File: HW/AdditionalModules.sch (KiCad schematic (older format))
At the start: 25 parts, among them J40 ph_1x2, Q40 BC817, Q41 BC817, U10 PCA9633DP1, U40 AT_CryptoAuth, U41 HIH8000_I2C

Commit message: Updates components to add manufacturer, part number, ... fields. Also checked some values.
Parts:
- C10: symbol Device:C -> calin:C; characteristics (none) -> 100 nF / 50V / X7R; manufacturer (none) -> Samsung; package (none) -> 0805; part-number (none) -> CL21B104KBCNNNC
- C11: value 1uF -> 4,7uF; symbol Device:C -> calin:C; characteristics (none) -> 4.7 µF / 16 V / X7R; manufacturer (none) -> AVX; package (none) -> 0805; part-number (none) -> 0805YC475KAT2A
- C40: symbol Device:C -> calin:C; Variant (none) -> ATCrypto; characteristics (none) -> 100 nF / 50V / X7R; manufacturer (none) -> Samsung; package (none) -> 0805; part-number (none) -> CL21B104KBCNNNC
- C41, C42: symbol Device:C -> calin:C; Variant (none) -> HIH; characteristics (none) -> 100 nF / 50V / X7R; manufacturer (none) -> Samsung; package (none) -> 0805; part-number (none) -> CL21B104KBCNNNC
- Q40, Q41: characteristics (none) -> BC817-40; manufacturer (none) -> Diodes; package (none) -> SOT-23; part-number (none) -> BC817-40Q
- R10, R11, R12, R13: characteristics (none) -> 100 1%; manufacturer (none) -> Panasonic; package (none) -> 0805; part-number (none) -> ERJ-6ENF1000V
- R40, R41: value 10K -> 10k; characteristics (none) -> 10k; manufacturer (none) -> Vishay; package (none) -> 0805; part-number (none) -> CRCW080510K0FKEA
- SYM10, SYM11, SYM12, SYM13: characteristics (none) -> LightPipe; manufacturer (none) -> BIVAR; package (none) -> SLP3-XXX-XXX-X; part-number (none) -> SLP3-150-xxx-F
- U10: characteristics (none) -> 4-bit Fm+ I2C-bus LED driver; manufacturer (none) -> NXP Semiconductors; package (none) -> TSSOP8 (SOT505-1); part-number (none) -> PCA9633DP1
- U40: Variant (none) -> ATCrypto; characteristics (none) -> *; manufacturer (none) -> Microchip; package (none) -> SOIC-8 3.90mm; part-number (none) -> ATSHA204A/ATECC508A/ATECC608A-SSHDA
- U41: Variant (none) -> HIH; characteristics (none) -> +/- 2.0 RH Accuracy; manufacturer (none) -> Honeywell; package (none) -> SOIC-8 3.90mm; part-number (none) -> HIH8130-021-001 / HIH8131-021-001
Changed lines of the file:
@@
 Sheet 3 3
 Title "ESP32 RFM69/RFM9x Gateway"
-Date "2019-04-25"
-Rev "32"
+Date "2019-05-02"
+Rev "33"
 Comp "Calin Radoni"
 Comment1 ""
@@
 F 2 "CalinGeneric:SOIC-8-HS" H 2200 4450 50  0001 C CNN
 F 3 "" H 2200 4450 50  0001 C CNN
+F 4 "ATCrypto" H 0   0   50  0001 C CNN "Variant"
+F 5 "ATSHA204A/ATECC508A/ATECC608A-SSHDA" H 0   0   50  0001 C CNN "part-number"
+F 6 "*" H 0   0   50  0001 C CNN "characteristics"
+F 7 "Microchip" H 0   0   50  0001 C CNN "manufacturer"
+F 8 "SOIC-8 3.90mm" H 0   0   50  0001 C CNN "package"
 	1    2200 4450
 	1    0    0    -1
 $EndComp
 $Comp
-L Device:C C?
+L calin:C C?
 U 1 1 5CCB0E9E
 P 1350 4450
@@
 F 2 "CalinGeneric:C0805HS" H 1388 4300 50  0001 C CNN
 F 3 "" H 1350 4450 50  0000 C CNN
+F 4 "ATCrypto" H 0   0   50  0001 C CNN "Variant"
+F 5 "100 nF / 50V / X7R" H 0   0   50  0001 C CNN "characteristics"
+F 6 "Samsung" H 0   0   50  0001 C CNN "manufacturer"
+F 7 "0805" H 0   0   50  0001 C CNN "package"
+F 8 "CL21B104KBCNNNC" H 0   0   50  0001 C CNN "part-number"
 	1    1350 4450
 	1    0    0    -1
@@
 F 2 "CalinGeneric:R0805HS" V 8430 1200 30  0001 C CNN
 F 3 "" H 8500 1200 30  0000 C CNN
+F 4 "100 1%" H 0   0   50  0001 C CNN "characteristics"
+F 5 "Panasonic" H 0   0   50  0001 C CNN "manufacturer"
+F 6 "0805" H 0   0   50  0001 C CNN "package"
+F 7 "ERJ-6ENF1000V" H 0   0   50  0001 C CNN "part-number"
 	1    8500 1200
 	0    1    1    0
@@
 F 2 "CalinGeneric:R0805HS" V 8430 1500 30  0001 C CNN
 F 3 "" H 8500 1500 30  0000 C CNN
+F 4 "100 1%" H 0   0   50  0001 C CNN "characteristics"
+F 5 "Panasonic" H 0   0   50  0001 C CNN "manufacturer"
+F 6 "0805" H 0   0   50  0001 C CNN "package"
+F 7 "ERJ-6ENF1000V" H 0   0   50  0001 C CNN "part-number"
 	1    8500 1500
 	0    1    1    0
@@
 F 2 "CalinGeneric:R0805HS" V 8430 1800 30  0001 C CNN
 F 3 "" H 8500 1800 30  0000 C CNN
+F 4 "100 1%" H 0   0   50  0001 C CNN "characteristics"
+F 5 "Panasonic" H 0   0   50  0001 C CNN "manufacturer"
+F 6 "0805" H 0   0   50  0001 C CNN "package"
+F 7 "ERJ-6ENF1000V" H 0   0   50  0001 C CNN "part-number"
 	1    8500 1800
 	0    1    1    0
@@
 F 2 "CalinGeneric:R0805HS" V 8430 2100 30  0001 C CNN
 F 3 "" H 8500 2100 30  0000 C CNN
+F 4 "100 1%" H 0   0   50  0001 C CNN "characteristics"
+F 5 "Panasonic" H 0   0   50  0001 C CNN "manufacturer"
+F 6 "0805" H 0   0   50  0001 C CNN "package"
+F 7 "ERJ-6ENF1000V" H 0   0   50  0001 C CNN "part-number"
 	1    8500 2100
 	0    1    1    0
@@
 F 2 "CalinGeneric:SLP3-xxx-150-x" H 9800 1200 50  0001 C CNN
 F 3 "" V 9800 1200 50  0001 C CNN
+F 4 "LightPipe" H 0   0   50  0001 C CNN "characteristics"
+F 5 "BIVAR" H 0   0   50  0001 C CNN "manufacturer"
+F 6 "SLP3-XXX-XXX-X" H 0   0   50  0001 C CNN "package"
+F 7 "SLP3-150-xxx-F" H 0   0   50  0001 C CNN "part-number"
 	1    9800 1200
 	1    0    0    -1
@@
 F 2 "CalinGeneric:SLP3-xxx-150-x" H 9800 1500 50  0001 C CNN
 F 3 "" V 9800 1500 50  0001 C CNN
+F 4 "LightPipe" H 0   0   50  0001 C CNN "characteristics"
+F 5 "BIVAR" H 0   0   50  0001 C CNN "manufacturer"
+F 6 "SLP3-XXX-XXX-X" H 0   0   50  0001 C CNN "package"
+F 7 "SLP3-150-xxx-F" H 0   0   50  0001 C CNN "part-number"
 	1    9800 1500
 	1    0    0    -1
@@
 F 2 "CalinGeneric:SLP3-xxx-150-x" H 9800 1800 50  0001 C CNN
 F 3 "" V 9800 1800 50  0001 C CNN
+F 4 "LightPipe" H 0   0   50  0001 C CNN "characteristics"
+F 5 "BIVAR" H 0   0   50  0001 C CNN "manufacturer"
+F 6 "SLP3-XXX-XXX-X" H 0   0   50  0001 C CNN "package"
+F 7 "SLP3-150-xxx-F" H 0   0   50  0001 C CNN "part-number"
 	1    9800 1800
 	1    0    0    -1
@@
 F 2 "CalinGeneric:SLP3-xxx-150-x" H 9800 2100 50  0001 C CNN
 F 3 "" V 9800 2100 50  0001 C CNN
+F 4 "LightPipe" H 0   0   50  0001 C CNN "characteristics"
+F 5 "BIVAR" H 0   0   50  0001 C CNN "manufacturer"
+F 6 "SLP3-XXX-XXX-X" H 0   0   50  0001 C CNN "package"
+F 7 "SLP3-150-xxx-F" H 0   0   50  0001 C CNN "part-number"
 	1    9800 2100
 	1    0    0    -1
@@
 AR Path="/5CCB086C/5CC095F4" Ref="R40"  Part="1"
 F 0 "R40" V 2280 6250 40  0000 C CNN
-F 1 "10K" V 2200 6250 40  0000 C CNN
+F 1 "10k" V 2200 6250 40  0000 C CNN
 F 2 "CalinGeneric:R0805HS" V 2130 6250 30  0001 C CNN
 F 3 "" H 2200 6250 30  0000 C CNN
+F 4 "10k" H 0   0   50  0001 C CNN "characteristics"
+F 5 "Vishay" H 0   0   50  0001 C CNN "manufacturer"
+F 6 "0805" H 0   0   50  0001 C CNN "package"
+F 7 "CRCW080510K0FKEA" H 0   0   50  0001 C CNN "part-number"
 	1    2200 6250
 	0    1    1    0
@@
 AR Path="/5CCB086C/5CC096FF" Ref="R41"  Part="1"
 F 0 "R41" V 2280 6850 40  0000 C CNN
-F 1 "10K" V 2200 6850 40  0000 C CNN
+F 1 "10k" V 2200 6850 40  0000 C CNN
 F 2 "CalinGeneric:R0805HS" V 2130 6850 30  0001 C CNN
 F 3 "" H 2200 6850 30  0000 C CNN
+F 4 "10k" H 0   0   50  0001 C CNN "characteristics"
+F 5 "Vishay" H 0   0   50  0001 C CNN "manufacturer"
+F 6 "0805" H 0   0   50  0001 C CNN "package"
+F 7 "CRCW080510K0FKEA" H 0   0   50  0001 C CNN "part-number"
 	1    2200 6850
 	0    1    1    0
@@
 F 1 "BC817" H 2841 6205 50  0000 L CNN
 F 2 "CalinGeneric:SOT-23" H 2850 6175 50  0001 L CIN
-F 3 "http://www.fairchildsemi.com/ds/BC/BC817.pdf" H 2650 6250 50  0001 L CNN
+F 3 "" H 2650 6250 50  0001 L CNN
+F 4 "BC817-40" H 0   0   50  0001 C CNN "characteristics"
+F 5 "Diodes" H 0   0   50  0001 C CNN "manufacturer"
+F 6 "SOT-23" H 0   0   50  0001 C CNN "package"
+F 7 "BC817-40Q" H 0   0   50  0001 C CNN "part-number"
 	1    2650 6250
 	1    0    0    -1
@@
 F 1 "BC817" H 2841 6895 50  0000 L CNN
 F 2 "CalinGeneric:SOT-23" H 2850 6775 50  0001 L CIN
-F 3 "http://www.fairchildsemi.com/ds/BC/BC817.pdf" H 2650 6850 50  0001 L CNN
+F 3 "" H 2650 6850 50  0001 L CNN
+F 4 "BC817-40" H 0   0   50  0001 C CNN "characteristics"
+F 5 "Diodes" H 0   0   50  0001 C CNN "manufacturer"
+F 6 "SOT-23" H 0   0   50  0001 C CNN "package"
+F 7 "BC817-40Q" H 0   0   50  0001 C CNN "part-number"
 	1    2650 6850
 	1    0    0    1
@@
 F 2 "CalinGeneric:TSSOP8-SOT505-1-HS" H 7700 1650 50  0001 C CNN
 F 3 "" H 7700 1650 50  0001 C CNN
+F 4 "4-bit Fm+ I2C-bus LED driver" H 0   0   50  0001 C CNN "characteristics"
+F 5 "NXP Semiconductors" H 0   0   50  0001 C CNN "manufacturer"
+F 6 "TSSOP8 (SOT505-1)" H 0   0   50  0001 C CNN "package"
+F 7 "PCA9633DP1" H 0   0   50  0001 C CNN "part-number"
 	1    7700 1650
 	-1   0    0    -1
 $EndComp
 $Comp
-L Device:C C?
+L calin:C C?
 U 1 1 5CBE9333
 P 6500 1650
@@
 F 2 "CalinGeneric:C0805HS" H 6538 1500 50  0001 C CNN
 F 3 "" H 6500 1650 50  0000 C CNN
+F 4 "100 nF / 50V / X7R" H 0   0   50  0001 C CNN "characteristics"
+F 5 "Samsung" H 0   0   50  0001 C CNN "manufacturer"
+F 6 "0805" H 0   0   50  0001 C CNN "package"
+F 7 "CL21B104KBCNNNC" H 0   0   50  0001 C CNN "part-number"
 	1    6500 1650
 	1    0    0    -1
@@
 F 2 "CalinGeneric:SOIC-8-HS" H 7700 5400 60  0001 C CNN
 F 3 "" H 7700 5400 60  0000 C CNN
+F 4 "HIH" H 0   0   50  0001 C CNN "Variant"
+F 5 "HIH8130-021-001 / HIH8131-021-001" H 0   0   50  0001 C CNN "part-number"
+F 6 "+/- 2.0 RH Accuracy" H 0   0   50  0001 C CNN "characteristics"
+F 7 "Honeywell" H 0   0   50  0001 C CNN "manufacturer"
+F 8 "SOIC-8 3.90mm" H 0   0   50  0001 C CNN "package"
 	1    7700 5400
 	1    0    0    -1
@@
 	7250 5350 7250 5750
 $Comp
-L Device:C C?
+L calin:C C?
 U 1 1 5CBF000C
 P 6500 5500
@@
 F 2 "CalinGeneric:C0805HS" H 6538 5350 50  0001 C CNN
 F 3 "" H 6500 5500 50  0000 C CNN
+F 4 "HIH" H 0   0   50  0001 C CNN "Variant"
+F 5 "100 nF / 50V / X7R" H 0   0   50  0001 C CNN "characteristics"
+F 6 "Samsung" H 0   0   50  0001 C CNN "manufacturer"
+F 7 "0805" H 0   0   50  0001 C CNN "package"
+F 8 "CL21B104KBCNNNC" H 0   0   50  0001 C CNN "part-number"
 	1    6500 5500
 	1    0    0    -1
 $EndComp
 $Comp
-L Device:C C?
+L calin:C C?
 U 1 1 5CBF00B7
 P 8400 5500
@@
 F 2 "CalinGeneric:C0805HS" H 8438 5350 50  0001 C CNN
 F 3 "" H 8400 5500 50  0000 C CNN
+F 4 "HIH" H 0   0   50  0001 C CNN "Variant"
+F 5 "100 nF / 50V / X7R" H 0   0   50  0001 C CNN "characteristics"
+F 6 "Samsung" H 0   0   50  0001 C CNN "manufacturer"
+F 7 "0805" H 0   0   50  0001 C CNN "package"
+F 8 "CL21B104KBCNNNC" H 0   0   50  0001 C CNN "part-number"
 	1    8400 5500
 	1    0    0    -1
@@
 	6500 5250 6500 5350
 $Comp
-L Device:C C?
+L calin:C C?
 U 1 1 5CC12D9F
 P 6150 1650
@@
 AR Path="/5CCB086C/5CC12D9F" Ref="C11"  Part="1"
 F 0 "C11" H 6175 1750 50  0000 L CNN
-F 1 "1uF" V 6200 1450 50  0000 L CNN
+F 1 "4,7uF" V 6200 1500 50  0000 C CNN
 F 2 "CalinGeneric:C0805HS" H 6188 1500 50  0001 C CNN
 F 3 "" H 6150 1650 50  0000 C CNN
+F 4 "4.7 µF / 16 V / X7R" H 0   0   50  0001 C CNN "characteristics"
+F 5 "AVX" H 0   0   50  0001 C CNN "manufacturer"
+F 6 "0805" H 0   0   50  0001 C CNN "package"
+F 7 "0805YC475KAT2A" H 0   0   50  0001 C CNN "part-number"
 	1    6150 1650
 	1    0    0    -1

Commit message: Changes C4 to NC to prevent unwanted boot to Download mode and removes keepout area from under the ESP32 module.
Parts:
- SYM10, SYM11, SYM12, SYM13: part-number SLP3-150-xxx-F -> SLP3-150-150-F
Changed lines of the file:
@@
 Title "ESP32 RFM69/RFM9x Gateway"
 Date "2019-05-02"
-Rev "33"
+Rev "34"
 Comp "Calin Radoni"
 Comment1 ""
@@
 F 5 "BIVAR" H 0   0   50  0001 C CNN "manufacturer"
 F 6 "SLP3-XXX-XXX-X" H 0   0   50  0001 C CNN "package"
-F 7 "SLP3-150-xxx-F" H 0   0   50  0001 C CNN "part-number"
+F 7 "SLP3-150-150-F" H 0   0   50  0001 C CNN "part-number"
 	1    9800 1200
 	1    0    0    -1
@@
 F 5 "BIVAR" H 0   0   50  0001 C CNN "manufacturer"
 F 6 "SLP3-XXX-XXX-X" H 0   0   50  0001 C CNN "package"
-F 7 "SLP3-150-xxx-F" H 0   0   50  0001 C CNN "part-number"
+F 7 "SLP3-150-150-F" H 0   0   50  0001 C CNN "part-number"
 	1    9800 1500
 	1    0    0    -1
@@
 F 5 "BIVAR" H 0   0   50  0001 C CNN "manufacturer"
 F 6 "SLP3-XXX-XXX-X" H 0   0   50  0001 C CNN "package"
-F 7 "SLP3-150-xxx-F" H 0   0   50  0001 C CNN "part-number"
+F 7 "SLP3-150-150-F" H 0   0   50  0001 C CNN "part-number"
 	1    9800 1800
 	1    0    0    -1
@@
 F 5 "BIVAR" H 0   0   50  0001 C CNN "manufacturer"
 F 6 "SLP3-XXX-XXX-X" H 0   0   50  0001 C CNN "package"
-F 7 "SLP3-150-xxx-F" H 0   0   50  0001 C CNN "part-number"
+F 7 "SLP3-150-150-F" H 0   0   50  0001 C CNN "part-number"
 	1    9800 2100
 	1    0    0    -1

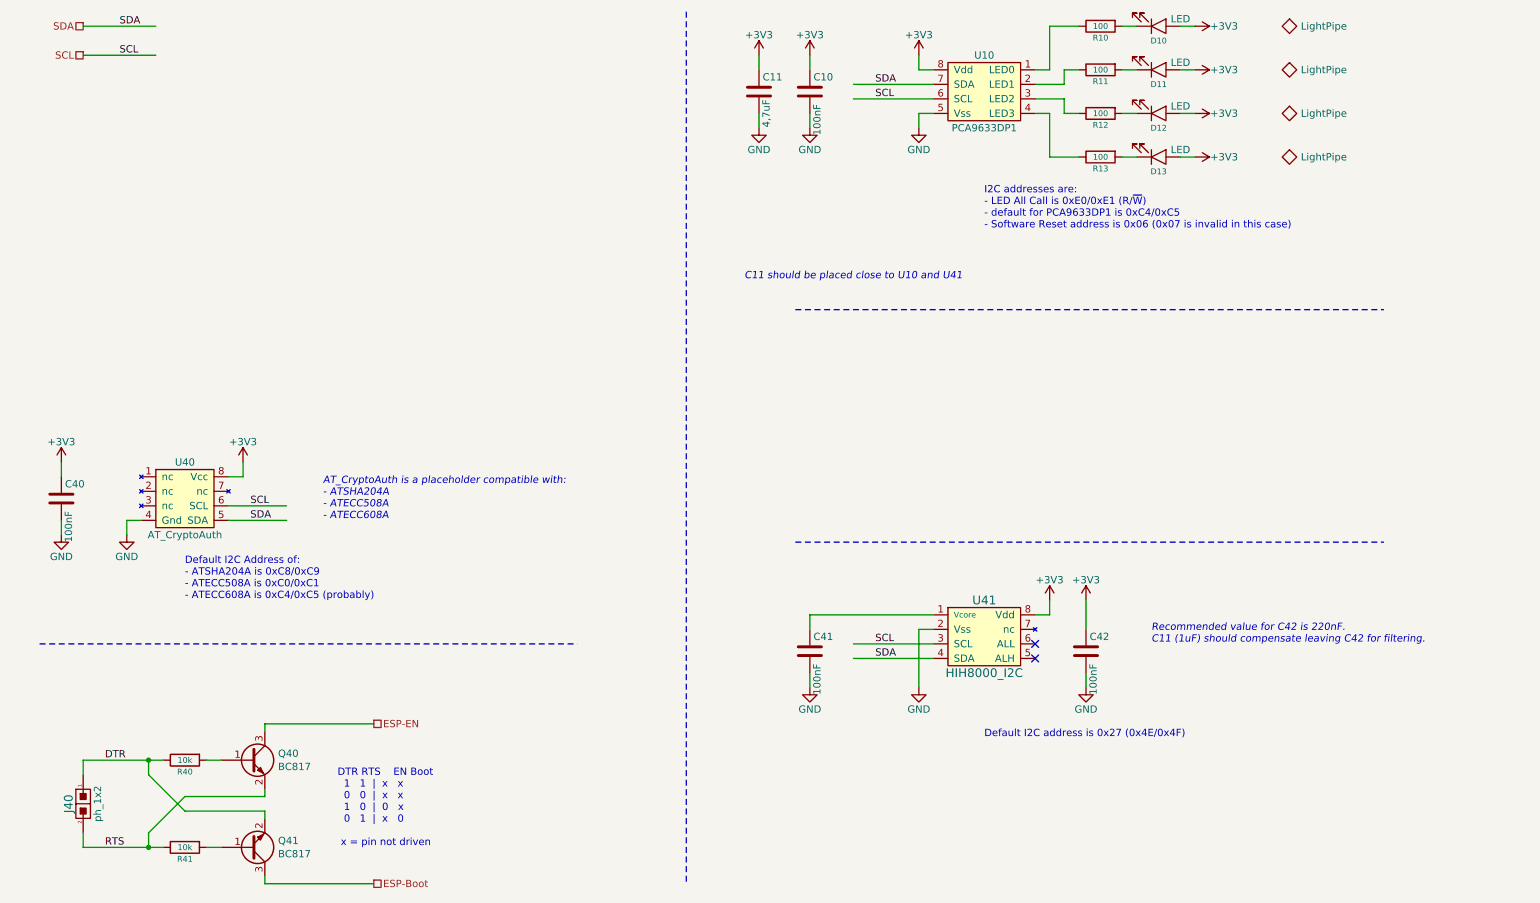
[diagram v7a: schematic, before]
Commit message: Connects the LEDs straight to ESP32, removing the LED driver.
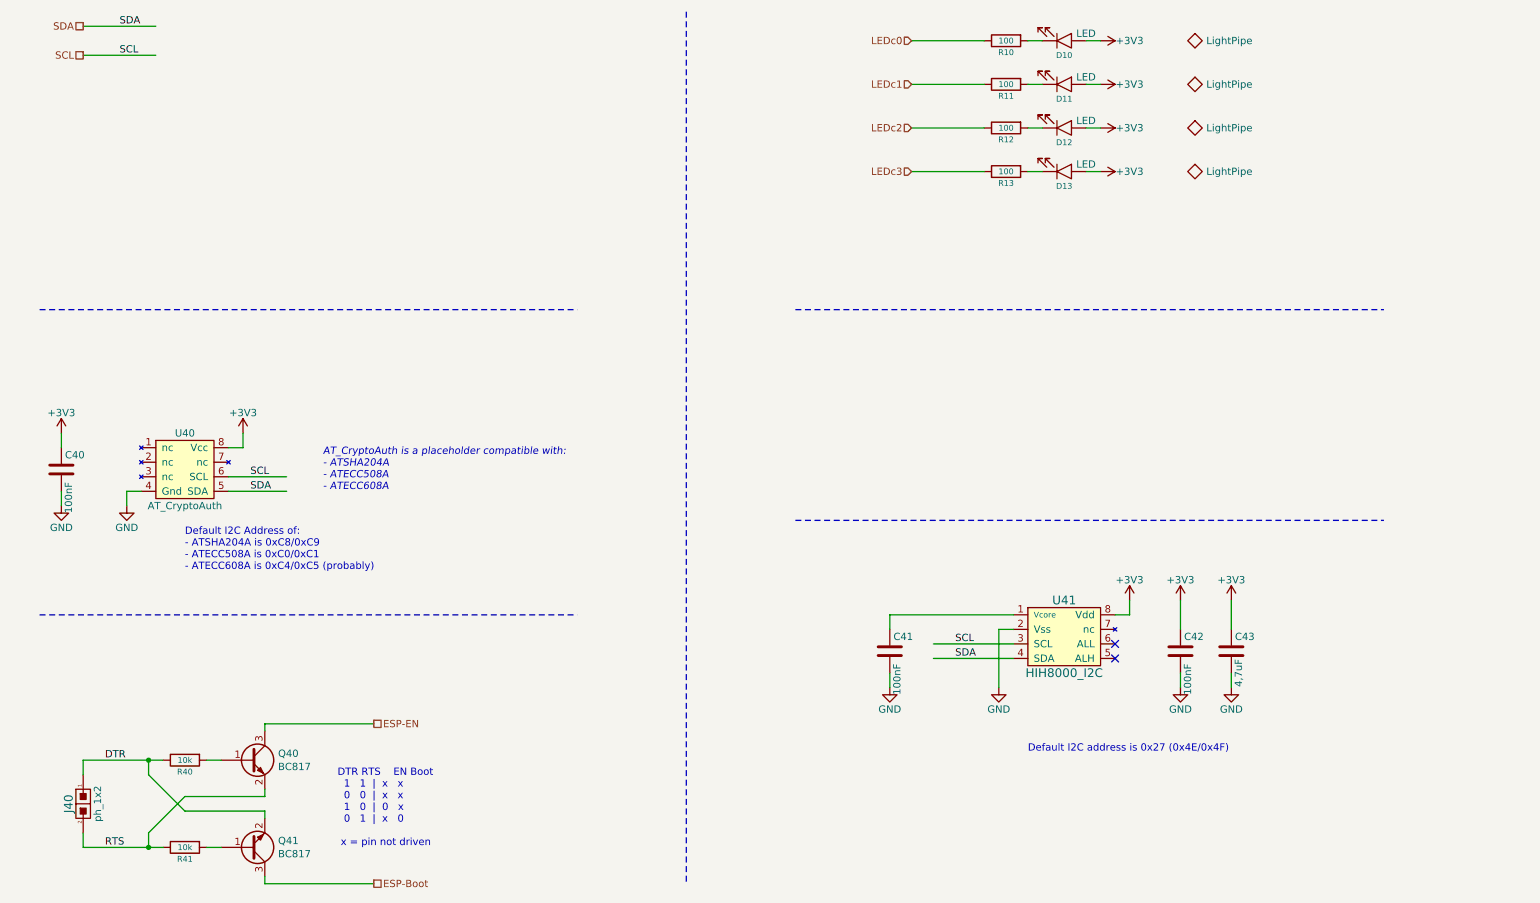
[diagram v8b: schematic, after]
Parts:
- removed C10: 100nF, CalinGeneric:C0805HS, symbol calin:C
- removed U10: PCA9633DP1, CalinGeneric:TSSOP8-SOT505-1-HS, symbol calin:PCA9633DP1
- renumbered C11 to C43
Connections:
- net labels added: LEDc0, LEDc1, LEDc2, LEDc3
- wire segments 71 -> 55
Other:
- note removed: "C11 should be placed close to U10 and U41"
- note removed: "I2C addresses are:\n- LED All Call is 0xE0/0xE1 (R/~W)\n- default for PCA9633DP1 is 0xC4/0xC5\n- Software Reset address is 0x06 (0x07 is invalid in this case)"
- note removed: "Recommended value for C42 is 220nF.\nC11 (1uF) should compensate leaving C42 for filtering."
- moved on the sheet: C40, C41, C42, C43, D10, D11, D12, D13, R10, R11, R12, R13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
